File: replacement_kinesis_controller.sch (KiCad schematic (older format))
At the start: 63 parts

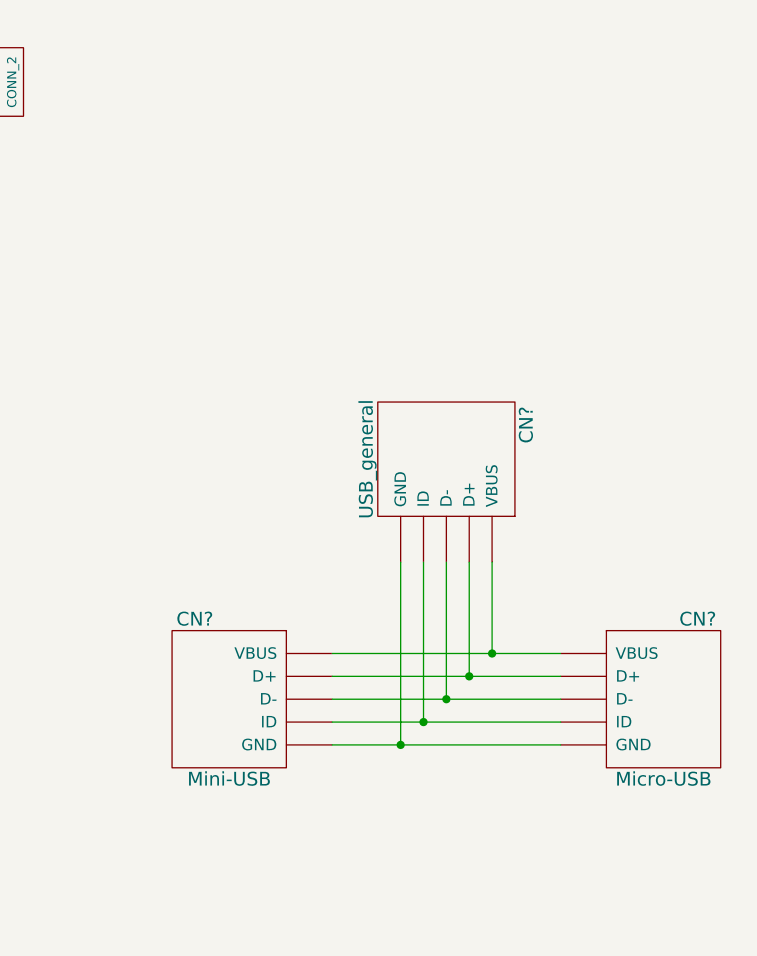
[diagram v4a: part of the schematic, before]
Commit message: Reorganize and fix USB breakout
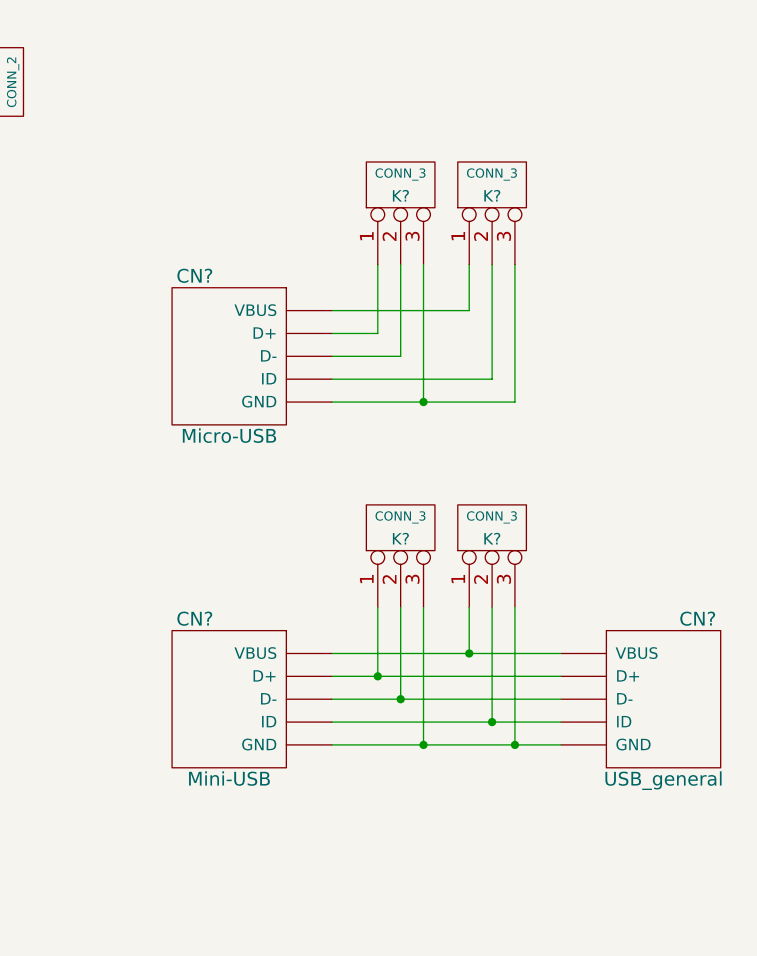
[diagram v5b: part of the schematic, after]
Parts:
- removed CN?: USB_general, symbol USB_general
- added CN?: USB_general, symbol USB_general
- added K? (x4): CONN_3, symbol CONN_3
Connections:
- net at CN?.~ (VBUS): now also CN?.~ (VBUS), K?.2 (PM); no longer CN?.~ (VBUS)
- net at CN?.~ (VBUS): now also K?.2 (PM); no longer CN?.~ (VBUS)
- new net: CN?.~ (VBUS), CN?.~ (VBUS), K?.1 (P1) (x2)
- new net: CN?.~ (VBUS), CN?.~ (VBUS), K?.2 (PM)
- new net: CN?.~ (VBUS), CN?.~ (VBUS), K?.3 (P3), K?.3 (P3)
- new net: CN?.~ (VBUS), K?.1 (P1) (x2)
- new net: CN?.~ (VBUS), K?.2 (PM)
- new net: CN?.~ (VBUS), K?.3 (P3), K?.3 (P3)
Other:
- moved on the sheet: CN?
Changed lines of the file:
@@
-$Comp
-L USB_general CN?
-U 1 1 54D67A64
-P 13500 450
-F 0 "CN?" H 13350 800 60  0000 C CNN
-F 1 "USB_general" H 13500 100 60  0000 C CNN
-F 2 "" H 13550 350 60  0000 C CNN
-F 3 "" H 13550 350 60  0000 C CNN
-	1    13500 450
-	0    1    1    0
-$EndComp
 $Comp
 L USB_general CN?
 U 1 1 54D67BF0
-P 14450 1500
-F 0 "CN?" H 14300 1850 60  0000 C CNN
-F 1 "Micro-USB" H 14450 1150 60  0000 C CNN
-F 2 "" H 14500 1400 60  0000 C CNN
-F 3 "" H 14500 1400 60  0000 C CNN
-	1    14450 1500
-	-1   0    0    -1
+P 12550 0
+F 0 "CN?" H 12400 350 60  0000 C CNN
+F 1 "Micro-USB" H 12550 -350 60  0000 C CNN
+F 2 "" H 12600 -100 60  0000 C CNN
+F 3 "" H 12600 -100 60  0000 C CNN
+	1    12550 0
+	1    0    0    -1
 $EndComp
 Wire Wire Line
@@
 Wire Wire Line
 	13000 1700 14000 1700
-Wire Wire Line
-	13300 900  13300 1700
-Connection ~ 13300 1700
-Wire Wire Line
-	13400 900  13400 1600
-Connection ~ 13400 1600
-Wire Wire Line
-	13500 900  13500 1500
-Connection ~ 13500 1500
-Wire Wire Line
-	13600 900  13600 1400
-Connection ~ 13600 1400
-Wire Wire Line
-	13700 900  13700 1300
-Connection ~ 13700 1300
 Text GLabel -300 -300 2    60   Input ~ 0
 PD2
@@
 Wire Wire Line
 	-600 -200 -300 -200
+$Comp
+L USB_general CN?
+U 1 1 54D71ECB
+P 14450 1500
+F 0 "CN?" H 14300 1850 60  0000 C CNN
+F 1 "USB_general" H 14450 1150 60  0000 C CNN
+F 2 "" H 14500 1400 60  0000 C CNN
+F 3 "" H 14500 1400 60  0000 C CNN
+	1    14450 1500
+	-1   0    0    -1
+$EndComp
+$Comp
+L CONN_3 K?
+U 1 1 54D72D0D
+P 13300 -750
+F 0 "K?" V 13250 -750 50  0000 C CNN
+F 1 "CONN_3" V 13350 -750 40  0000 C CNN
+F 2 "" H 13300 -750 60  0000 C CNN
+F 3 "" H 13300 -750 60  0000 C CNN
+	1    13300 -750
+	0    -1   -1   0
+$EndComp
+$Comp
+L CONN_3 K?
+U 1 1 54D72DB4
+P 13700 -750
+F 0 "K?" V 13650 -750 50  0000 C CNN
+F 1 "CONN_3" V 13750 -750 40  0000 C CNN
+F 2 "" H 13700 -750 60  0000 C CNN
+F 3 "" H 13700 -750 60  0000 C CNN
+	1    13700 -750
+	0    -1   -1   0
+$EndComp
+$Comp
+L CONN_3 K?
+U 1 1 54D7305D
+P 13300 750
+F 0 "K?" V 13250 750 50  0000 C CNN
+F 1 "CONN_3" V 13350 750 40  0000 C CNN
+F 2 "" H 13300 750 60  0000 C CNN
+F 3 "" H 13300 750 60  0000 C CNN
+	1    13300 750
+	0    -1   -1   0
+$EndComp
+$Comp
+L CONN_3 K?
+U 1 1 54D73063
+P 13700 750
+F 0 "K?" V 13650 750 50  0000 C CNN
+F 1 "CONN_3" V 13750 750 40  0000 C CNN
+F 2 "" H 13700 750 60  0000 C CNN
+F 3 "" H 13700 750 60  0000 C CNN
+	1    13700 750
+	0    -1   -1   0
+$EndComp
+Wire Wire Line
+	13200 -400 13200 -100
+Wire Wire Line
+	13200 -100 13000 -100
+Wire Wire Line
+	13300 -400 13300 0
+Wire Wire Line
+	13300 0    13000 0
+Wire Wire Line
+	13400 -400 13400 200
+Wire Wire Line
+	13000 200  13800 200
+Wire Wire Line
+	13600 -400 13600 -200
+Wire Wire Line
+	13600 -200 13000 -200
+Wire Wire Line
+	13700 -400 13700 100
+Wire Wire Line
+	13700 100  13000 100
+Wire Wire Line
+	13800 200  13800 -400
+Connection ~ 13400 200
+Wire Wire Line
+	13200 1100 13200 1400
+Connection ~ 13200 1400
+Wire Wire Line
+	13300 1100 13300 1500
+Connection ~ 13300 1500
+Wire Wire Line
+	13400 1100 13400 1700
+Connection ~ 13400 1700
+Wire Wire Line
+	13600 1100 13600 1300
+Connection ~ 13600 1300
+Wire Wire Line
+	13700 1100 13700 1600
+Connection ~ 13700 1600
+Wire Wire Line
+	13800 1100 13800 1700
+Connection ~ 13800 1700
 $EndSCHEMATC

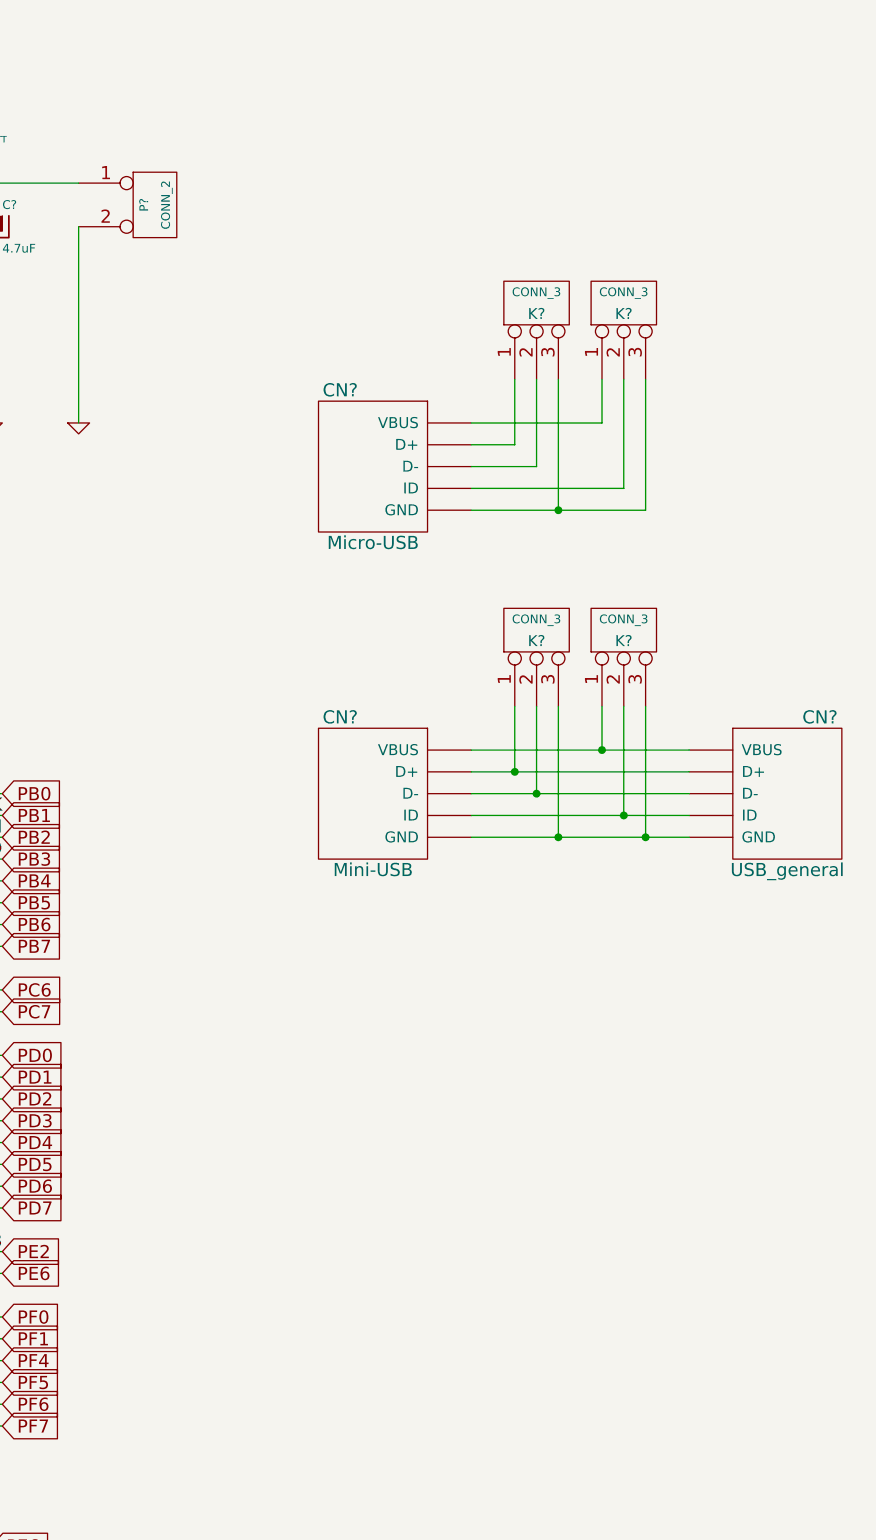
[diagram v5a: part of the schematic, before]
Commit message: Add battery guage circuitry
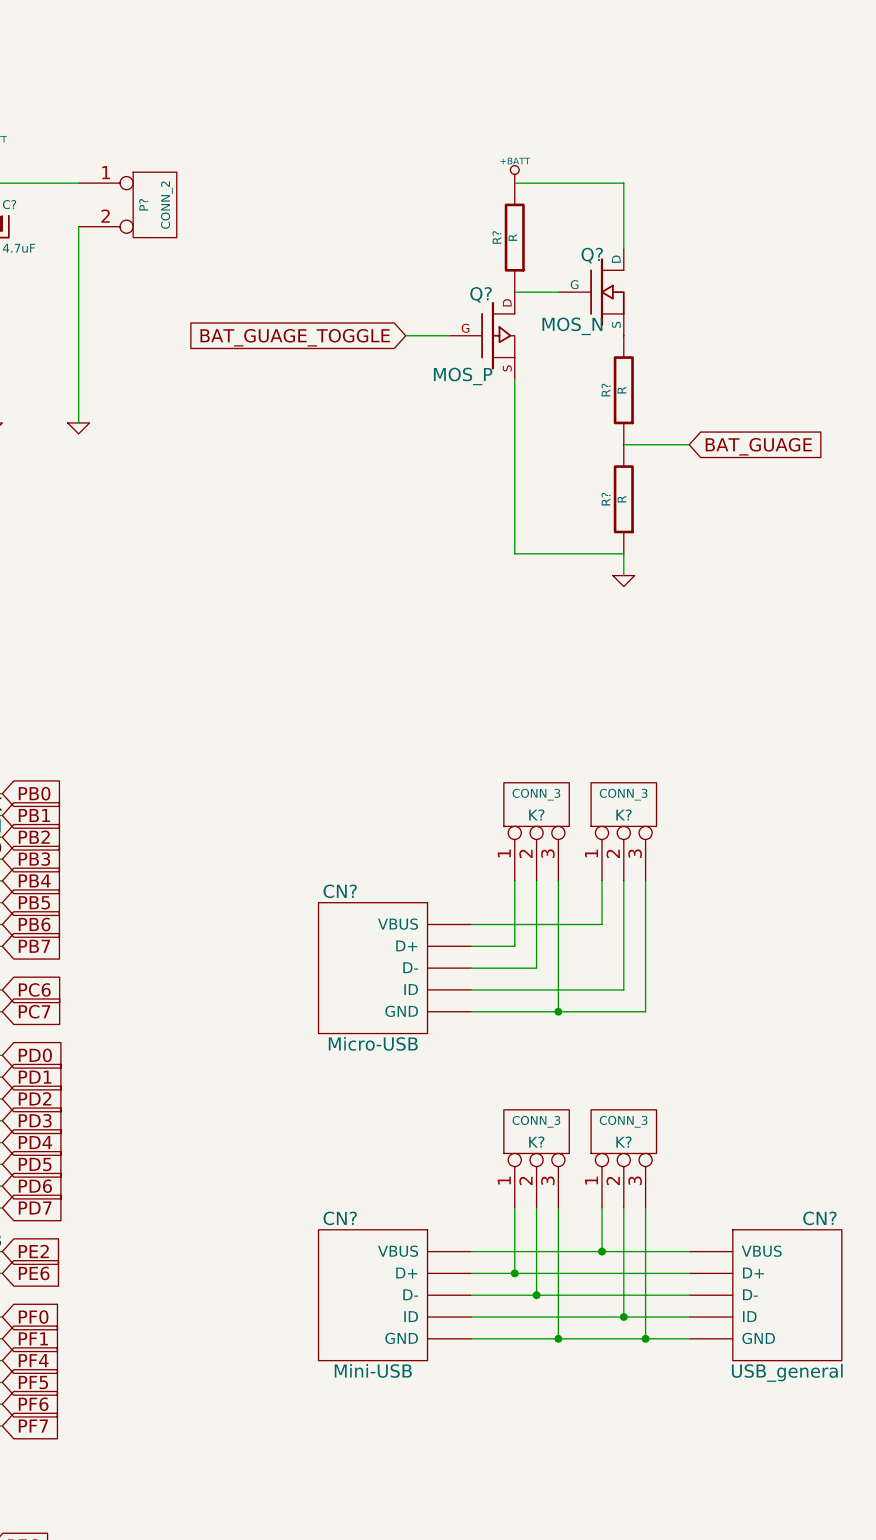
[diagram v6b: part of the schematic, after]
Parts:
- added Q?: MOS_P, symbol MOS_P
- added Q?: MOS_N, symbol MOS_N
- added R? (x3): R, symbol R
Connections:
- net +BATT: now also Q?.D, R?.2
- net GND: now also Q?.S, R?.1
- net at CN?.~ (VBUS), CN?.~ (VBUS): now also K?.2 (PM); no longer K?.1 (P1)
- new net: CN?.~ (VBUS), CN?.~ (VBUS), K?.1 (P1) (x2)
- new net: CN?.~ (VBUS), CN?.~ (VBUS), K?.2 (PM)
- new net: Q?.D, Q?.G, R?.1
- new net: Q?.S, R?.2
- new net BAT_GUAGE: R?.1, R?.2
- new net BAT_GUAGE_TOGGLE: Q?.G
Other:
- moved on the sheet: CN?, K?
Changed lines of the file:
@@
 L USB_general CN?
 U 1 1 54D6702A
-P 12550 1500
-F 0 "CN?" H 12400 1850 60  0000 C CNN
-F 1 "Mini-USB" H 12550 1150 60  0000 C CNN
-F 2 "" H 12600 1400 60  0000 C CNN
-F 3 "" H 12600 1400 60  0000 C CNN
-	1    12550 1500
+P 12550 3800
+F 0 "CN?" H 12400 4150 60  0000 C CNN
+F 1 "Mini-USB" H 12550 3450 60  0000 C CNN
+F 2 "" H 12600 3700 60  0000 C CNN
+F 3 "" H 12600 3700 60  0000 C CNN
+	1    12550 3800
 	1    0    0    -1
 $EndComp
@@
 L USB_general CN?
 U 1 1 54D67BF0
-P 12550 0
-F 0 "CN?" H 12400 350 60  0000 C CNN
-F 1 "Micro-USB" H 12550 -350 60  0000 C CNN
-F 2 "" H 12600 -100 60  0000 C CNN
-F 3 "" H 12600 -100 60  0000 C CNN
-	1    12550 0
+P 12550 2300
+F 0 "CN?" H 12400 2650 60  0000 C CNN
+F 1 "Micro-USB" H 12550 1950 60  0000 C CNN
+F 2 "" H 12600 2200 60  0000 C CNN
+F 3 "" H 12600 2200 60  0000 C CNN
+	1    12550 2300
 	1    0    0    -1
 $EndComp
@@
 	7600 4800 7600 4700
 Wire Wire Line
-	13000 1300 14000 1300
-Wire Wire Line
-	14000 1400 13000 1400
-Wire Wire Line
-	13000 1500 14000 1500
-Wire Wire Line
-	14000 1600 13000 1600
-Wire Wire Line
-	13000 1700 14000 1700
+	13000 3600 14000 3600
+Wire Wire Line
+	14000 3700 13000 3700
+Wire Wire Line
+	13000 3800 14000 3800
+Wire Wire Line
+	14000 3900 13000 3900
+Wire Wire Line
+	13000 4000 14000 4000
 Text GLabel -300 -300 2    60   Input ~ 0
 PD2
@@
 L USB_general CN?
 U 1 1 54D71ECB
-P 14450 1500
-F 0 "CN?" H 14300 1850 60  0000 C CNN
-F 1 "USB_general" H 14450 1150 60  0000 C CNN
-F 2 "" H 14500 1400 60  0000 C CNN
-F 3 "" H 14500 1400 60  0000 C CNN
-	1    14450 1500
+P 14450 3800
+F 0 "CN?" H 14300 4150 60  0000 C CNN
+F 1 "USB_general" H 14450 3450 60  0000 C CNN
+F 2 "" H 14500 3700 60  0000 C CNN
+F 3 "" H 14500 3700 60  0000 C CNN
+	1    14450 3800
 	-1   0    0    -1
 $EndComp
@@
 L CONN_3 K?
 U 1 1 54D72D0D
-P 13300 -750
-F 0 "K?" V 13250 -750 50  0000 C CNN
-F 1 "CONN_3" V 13350 -750 40  0000 C CNN
-F 2 "" H 13300 -750 60  0000 C CNN
-F 3 "" H 13300 -750 60  0000 C CNN
-	1    13300 -750
+P 13300 1550
+F 0 "K?" V 13250 1550 50  0000 C CNN
+F 1 "CONN_3" V 13350 1550 40  0000 C CNN
+F 2 "" H 13300 1550 60  0000 C CNN
+F 3 "" H 13300 1550 60  0000 C CNN
+	1    13300 1550
 	0    -1   -1   0
 $EndComp
@@
 L CONN_3 K?
 U 1 1 54D72DB4
-P 13700 -750
-F 0 "K?" V 13650 -750 50  0000 C CNN
-F 1 "CONN_3" V 13750 -750 40  0000 C CNN
-F 2 "" H 13700 -750 60  0000 C CNN
-F 3 "" H 13700 -750 60  0000 C CNN
-	1    13700 -750
+P 13700 1550
+F 0 "K?" V 13650 1550 50  0000 C CNN
+F 1 "CONN_3" V 13750 1550 40  0000 C CNN
+F 2 "" H 13700 1550 60  0000 C CNN
+F 3 "" H 13700 1550 60  0000 C CNN
+	1    13700 1550
 	0    -1   -1   0
 $EndComp
@@
 L CONN_3 K?
 U 1 1 54D7305D
-P 13300 750
-F 0 "K?" V 13250 750 50  0000 C CNN
-F 1 "CONN_3" V 13350 750 40  0000 C CNN
-F 2 "" H 13300 750 60  0000 C CNN
-F 3 "" H 13300 750 60  0000 C CNN
-	1    13300 750
+P 13300 3050
+F 0 "K?" V 13250 3050 50  0000 C CNN
+F 1 "CONN_3" V 13350 3050 40  0000 C CNN
+F 2 "" H 13300 3050 60  0000 C CNN
+F 3 "" H 13300 3050 60  0000 C CNN
+	1    13300 3050
 	0    -1   -1   0
 $EndComp
@@
 L CONN_3 K?
 U 1 1 54D73063
-P 13700 750
-F 0 "K?" V 13650 750 50  0000 C CNN
-F 1 "CONN_3" V 13750 750 40  0000 C CNN
-F 2 "" H 13700 750 60  0000 C CNN
-F 3 "" H 13700 750 60  0000 C CNN
-	1    13700 750
+P 13700 3050
+F 0 "K?" V 13650 3050 50  0000 C CNN
+F 1 "CONN_3" V 13750 3050 40  0000 C CNN
+F 2 "" H 13700 3050 60  0000 C CNN
+F 3 "" H 13700 3050 60  0000 C CNN
+	1    13700 3050
 	0    -1   -1   0
 $EndComp
 Wire Wire Line
-	13200 -400 13200 -100
-Wire Wire Line
-	13200 -100 13000 -100
-Wire Wire Line
-	13300 -400 13300 0
-Wire Wire Line
-	13300 0    13000 0
-Wire Wire Line
-	13400 -400 13400 200
-Wire Wire Line
-	13000 200  13800 200
-Wire Wire Line
-	13600 -400 13600 -200
-Wire Wire Line
-	13600 -200 13000 -200
-Wire Wire Line
-	13700 -400 13700 100
-Wire Wire Line
-	13700 100  13000 100
-Wire Wire Line
-	13800 200  13800 -400
-Connection ~ 13400 200
-Wire Wire Line
-	13200 1100 13200 1400
-Connection ~ 13200 1400
-Wire Wire Line
-	13300 1100 13300 1500
-Connection ~ 13300 1500
-Wire Wire Line
-	13400 1100 13400 1700
-Connection ~ 13400 1700
-Wire Wire Line
-	13600 1100 13600 1300
-Connection ~ 13600 1300
-Wire Wire Line
-	13700 1100 13700 1600
-Connection ~ 13700 1600
-Wire Wire Line
-	13800 1100 13800 1700
-Connection ~ 13800 1700
+	13200 1900 13200 2200
+Wire Wire Line
+	13200 2200 13000 2200
+Wire Wire Line
+	13300 1900 13300 2300
+Wire Wire Line
+	13300 2300 13000 2300
+Wire Wire Line
+	13400 1900 13400 2500
+Wire Wire Line
+	13000 2500 13800 2500
+Wire Wire Line
+	13600 1900 13600 2100
+Wire Wire Line
+	13600 2100 13000 2100
+Wire Wire Line
+	13700 1900 13700 2400
+Wire Wire Line
+	13700 2400 13000 2400
+Wire Wire Line
+	13800 2500 13800 1900
+Connection ~ 13400 2500
+Wire Wire Line
+	13200 3400 13200 3700
+Connection ~ 13200 3700
+Wire Wire Line
+	13300 3400 13300 3800
+Connection ~ 13300 3800
+Wire Wire Line
+	13400 3400 13400 4000
+Connection ~ 13400 4000
+Wire Wire Line
+	13600 3400 13600 3600
+Connection ~ 13600 3600
+Wire Wire Line
+	13700 3400 13700 3900
+Connection ~ 13700 3900
+Wire Wire Line
+	13800 3400 13800 4000
+Connection ~ 13800 4000
+$Comp
+L MOS_P Q?
+U 1 1 54D76FE9
+P 13100 -600
+F 0 "Q?" H 13100 -410 60  0000 R CNN
+F 1 "MOS_P" H 13100 -780 60  0000 R CNN
+F 2 "" H 13100 -600 60  0000 C CNN
+F 3 "" H 13100 -600 60  0000 C CNN
+	1    13100 -600
+	1    0    0    -1
+$EndComp
+$Comp
+L MOS_N Q?
+U 1 1 54D7703E
+P 13600 -800
+F 0 "Q?" H 13610 -630 60  0000 R CNN
+F 1 "MOS_N" H 13610 -950 60  0000 R CNN
+F 2 "" H 13600 -800 60  0000 C CNN
+F 3 "" H 13600 -800 60  0000 C CNN
+	1    13600 -800
+	1    0    0    -1
+$EndComp
+$Comp
+L R R?
+U 1 1 54D7937A
+P 13200 -1050
+F 0 "R?" V 13280 -1050 40  0000 C CNN
+F 1 "R" V 13207 -1049 40  0000 C CNN
+F 2 "" V 13130 -1050 30  0000 C CNN
+F 3 "" H 13200 -1050 30  0000 C CNN
+	1    13200 -1050
+	-1   0    0    1
+$EndComp
+$Comp
+L R R?
+U 1 1 54D79466
+P 13700 -350
+F 0 "R?" V 13780 -350 40  0000 C CNN
+F 1 "R" V 13707 -349 40  0000 C CNN
+F 2 "" V 13630 -350 30  0000 C CNN
+F 3 "" H 13700 -350 30  0000 C CNN
+	1    13700 -350
+	-1   0    0    1
+$EndComp
+$Comp
+L R R?
+U 1 1 54D794F1
+P 13700 150
+F 0 "R?" V 13780 150 40  0000 C CNN
+F 1 "R" V 13707 151 40  0000 C CNN
+F 2 "" V 13630 150 30  0000 C CNN
+F 3 "" H 13700 150 30  0000 C CNN
+	1    13700 150
+	-1   0    0    1
+$EndComp
+Wire Wire Line
+	13200 -800 13400 -800
+Wire Wire Line
+	13200 -400 13200 400
+Wire Wire Line
+	13200 400  13700 400
+Wire Wire Line
+	13700 -1000 13700 -1300
+Wire Wire Line
+	13700 -1300 13200 -1300
+Text GLabel 14000 -100 2    60   Input ~ 0
+BAT_GUAGE
+Text GLabel 12700 -600 0    60   Input ~ 0
+BAT_GUAGE_TOGGLE
+Wire Wire Line
+	12700 -600 12900 -600
+Wire Wire Line
+	13700 -100 14000 -100
+$Comp
+L +BATT #PWR?
+U 1 1 54D7A46B
+P 13200 -1300
+F 0 "#PWR?" H 13200 -1350 20  0001 C CNN
+F 1 "+BATT" H 13200 -1200 30  0000 C CNN
+F 2 "" H 13200 -1300 60  0000 C CNN
+F 3 "" H 13200 -1300 60  0000 C CNN
+	1    13200 -1300
+	1    0    0    -1
+$EndComp
+$Comp
+L GND #PWR?
+U 1 1 54D7A4BE
+P 13700 500
+F 0 "#PWR?" H 13700 500 30  0001 C CNN
+F 1 "GND" H 13700 430 30  0001 C CNN
+F 2 "" H 13700 500 60  0000 C CNN
+F 3 "" H 13700 500 60  0000 C CNN
+	1    13700 500
+	1    0    0    -1
+$EndComp
+Wire Wire Line
+	13700 400  13700 500
 $EndSCHEMATC
